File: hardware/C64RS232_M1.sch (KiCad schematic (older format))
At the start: 9 parts, among them J1 C64 USER PORT, J2 DE-9 FEMALE / DTE, U1 MAX3243

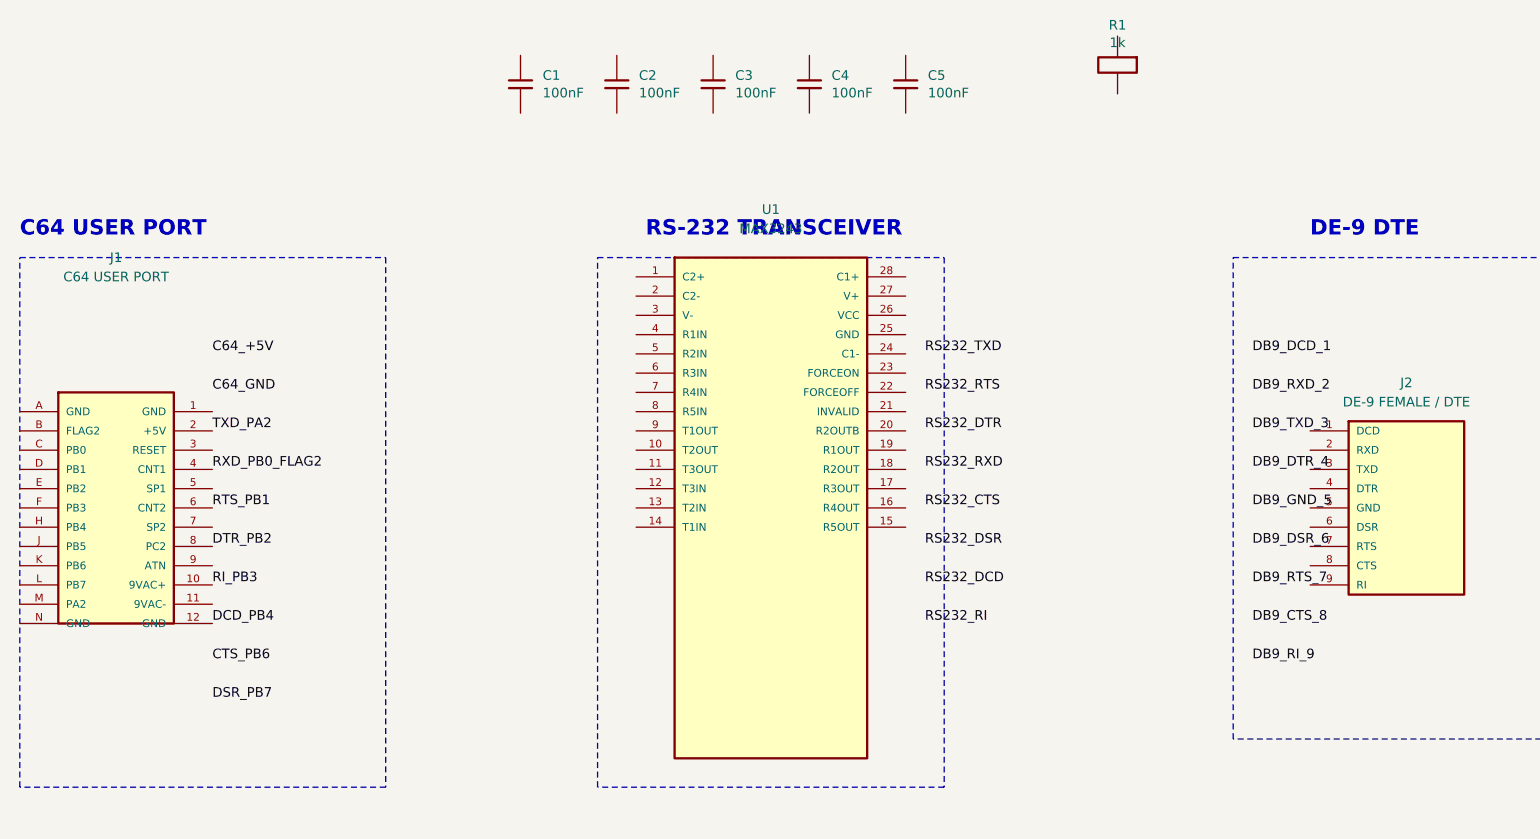
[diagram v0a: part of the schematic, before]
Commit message: Generate electrically connected KiCad M1.8 schematic
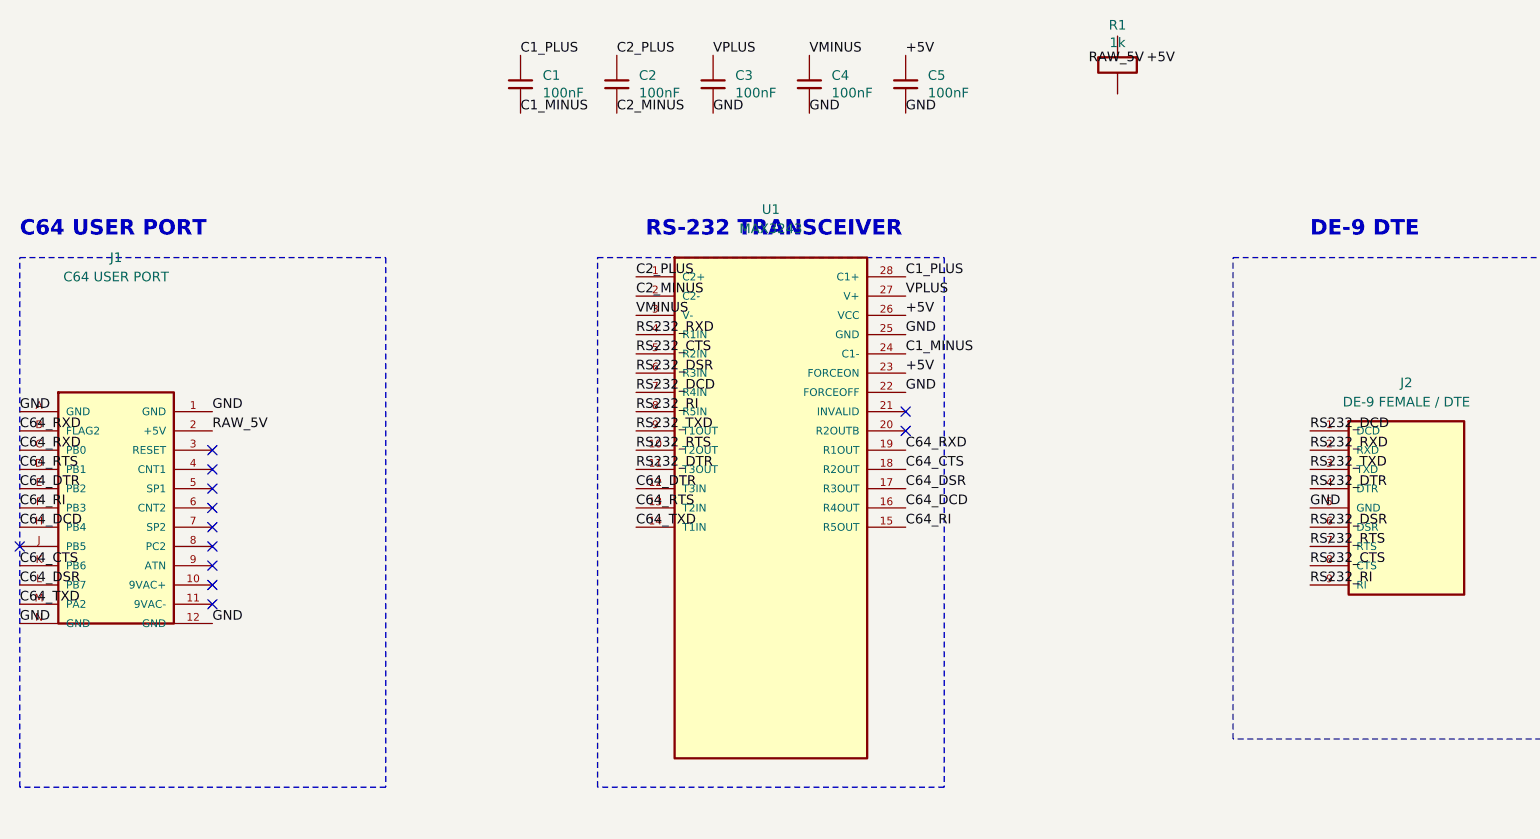
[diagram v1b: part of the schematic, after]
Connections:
- net DCD_PB4 is gone; now on net GND: J1.12 (GND)
- net RS232_CTS: now also J2.8 (CTS), U1.5 (R2IN)
- net RS232_DCD: now also J2.1 (DCD), U1.7 (R4IN)
- net RS232_DSR: now also J2.6 (DSR), U1.6 (R3IN)
- net RS232_DTR: now also J2.4 (DTR), U1.11 (T3OUT)
- net RS232_RI: now also J2.9 (RI), U1.8 (R5IN)
- net RS232_RTS: now also J2.7 (RTS), U1.10 (T2OUT)
- net RS232_RXD: now also J2.2 (RXD), U1.4 (R1IN)
- net RS232_TXD: now also J2.3 (TXD), U1.9 (T1OUT)
- net GND: now reaches J1.1 (GND)
- net GND: now also C3.2, C4.2, C5.2, J1.A (GND), J1.N (GND), J2.5 (GND), U1.22 (FORCEOFF), U1.25 (GND)
- net C64_RXD: now reaches J1.B (FLAG2)
- net C64_RXD: now also J1.C (PB0), U1.19 (R1OUT)
- net C64_RTS: now reaches J1.D (PB1)
- net C64_RTS: now also U1.13 (T2IN)
- net C64_DTR: now reaches J1.E (PB2)
- net C64_DTR: now also U1.12 (T3IN)
- net C64_RI: now reaches J1.F (PB3)
- net C64_RI: now also U1.15 (R5OUT)
- net C64_DCD: now reaches J1.H (PB4)
- net C64_DCD: now also U1.16 (R4OUT)
- net C64_CTS: now reaches J1.K (PB6)
- net C64_CTS: now also U1.18 (R2OUT)
- net C64_DSR: now reaches J1.L (PB7)
- net C64_DSR: now also U1.17 (R3OUT)
- net C64_TXD: now reaches J1.M (PA2)
- net C64_TXD: now also U1.14 (T1IN)
- net C2_PLUS: now reaches U1.1 (C2+)
- net C2_PLUS: now also C2.1
- net C2_MINUS: now reaches U1.2 (C2-)
- net C2_MINUS: now also C2.2
- net +5V: now reaches U1.23 (FORCEON)
- net +5V: now also C5.1, U1.26 (VCC)
- net C1_MINUS: now reaches U1.24 (C1-)
- net C1_MINUS: now also C1.2
- net VPLUS: now reaches U1.27 (V+)
- net VPLUS: now also C3.1
- net C1_PLUS: now reaches U1.28 (C1+)
- net C1_PLUS: now also C1.1
- net VMINUS: now reaches U1.3 (V-)
- net VMINUS: now also C4.1
- net DTR_PB2: no longer names the net of J1.8 (PC2)
- net RI_PB3: no longer names the net of J1.10 (9VAC+)
- net RTS_PB1: no longer names the net of J1.6 (CNT2)
- net RXD_PB0_FLAG2: no longer names the net of J1.4 (CNT1)
- net TXD_PA2 renamed RAW_5V
- no-connect marks 0 -> 12
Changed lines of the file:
@@
 Title "C64RS232 User Port to RS-232"
 Date "2026-09-14"
-Rev "M1"
+Rev "M1.8"
 Comp "Ploos-AS"
 Comment1 "C64 User Port / MAX3243 / DE-9 DTE"
 Comment2 "SLIP-capable architecture"
-Comment3 "M1 schematic baseline"
+Comment3 "M1.8 electrically connected baseline"
 Comment4 "Verify against datasheets before manufacture"
 $EndDescr
@@
 Text Notes 1400 6200 0 60 ~ 12
 This is an M1 design baseline; ERC/DRC and manufacturer-specific footprint checks remain required.
-Text Label 2300 3000 0 50 ~ 0
-C64_+5V
-Text Label 2300 3200 0 50 ~ 0
-C64_GND
+Text Label 1300 4300 0 50 ~ 0
+C64_TXD
+Text Label 4500 3900 0 50 ~ 0
+C64_TXD
+Text Label 1300 3600 0 50 ~ 0
+C64_RTS
+Text Label 4500 3800 0 50 ~ 0
+C64_RTS
+Text Label 1300 3700 0 50 ~ 0
+C64_DTR
+Text Label 4500 3700 0 50 ~ 0
+C64_DTR
+Text Label 1300 3500 0 50 ~ 0
+C64_RXD
+Text Label 1300 3400 0 50 ~ 0
+C64_RXD
+Text Label 5900 3500 0 50 ~ 0
+C64_RXD
+Text Label 1300 4100 0 50 ~ 0
+C64_CTS
+Text Label 5900 3600 0 50 ~ 0
+C64_CTS
+Text Label 1300 4200 0 50 ~ 0
+C64_DSR
+Text Label 5900 3700 0 50 ~ 0
+C64_DSR
+Text Label 1300 3900 0 50 ~ 0
+C64_DCD
+Text Label 5900 3800 0 50 ~ 0
+C64_DCD
+Text Label 1300 3800 0 50 ~ 0
+C64_RI
+Text Label 5900 3900 0 50 ~ 0
+C64_RI
+Text Label 4500 3400 0 50 ~ 0
+RS232_TXD
+Text Label 8000 3600 0 50 ~ 0
+RS232_TXD
+Text Label 4500 3500 0 50 ~ 0
+RS232_RTS
+Text Label 8000 4000 0 50 ~ 0
+RS232_RTS
+Text Label 4500 3600 0 50 ~ 0
+RS232_DTR
+Text Label 8000 3700 0 50 ~ 0
+RS232_DTR
+Text Label 4500 2900 0 50 ~ 0
+RS232_RXD
+Text Label 8000 3500 0 50 ~ 0
+RS232_RXD
+Text Label 4500 3000 0 50 ~ 0
+RS232_CTS
+Text Label 8000 4100 0 50 ~ 0
+RS232_CTS
+Text Label 4500 3100 0 50 ~ 0
+RS232_DSR
+Text Label 8000 3900 0 50 ~ 0
+RS232_DSR
+Text Label 4500 3200 0 50 ~ 0
+RS232_DCD
+Text Label 8000 3400 0 50 ~ 0
+RS232_DCD
+Text Label 4500 3300 0 50 ~ 0
+RS232_RI
+Text Label 8000 4200 0 50 ~ 0
+RS232_RI
 Text Label 2300 3400 0 50 ~ 0
-TXD_PA2
-Text Label 2300 3600 0 50 ~ 0
-RXD_PB0_FLAG2
-Text Label 2300 3800 0 50 ~ 0
-RTS_PB1
-Text Label 2300 4000 0 50 ~ 0
-DTR_PB2
-Text Label 2300 4200 0 50 ~ 0
-RI_PB3
+RAW_5V
+Text Label 6850 1500 0 50 ~ 0
+RAW_5V
+Text Label 7150 1500 0 50 ~ 0
++5V
+Text Label 5900 2800 0 50 ~ 0
++5V
+Text Label 5900 3100 0 50 ~ 0
++5V
+Text Label 5900 1450 0 50 ~ 0
++5V
+Text Label 2300 3300 0 50 ~ 0
+GND
 Text Label 2300 4400 0 50 ~ 0
-DCD_PB4
-Text Label 2300 4600 0 50 ~ 0
-CTS_PB6
-Text Label 2300 4800 0 50 ~ 0
-DSR_PB7
-Text Label 6000 3000 0 50 ~ 0
-RS232_TXD
-Text Label 6000 3200 0 50 ~ 0
-RS232_RTS
-Text Label 6000 3400 0 50 ~ 0
-RS232_DTR
-Text Label 6000 3600 0 50 ~ 0
-RS232_RXD
-Text Label 6000 3800 0 50 ~ 0
-RS232_CTS
-Text Label 6000 4000 0 50 ~ 0
-RS232_DSR
-Text Label 6000 4200 0 50 ~ 0
-RS232_DCD
-Text Label 6000 4400 0 50 ~ 0
-RS232_RI
-Text Label 7700 3000 0 50 ~ 0
-DB9_DCD_1
-Text Label 7700 3200 0 50 ~ 0
-DB9_RXD_2
-Text Label 7700 3400 0 50 ~ 0
-DB9_TXD_3
-Text Label 7700 3600 0 50 ~ 0
-DB9_DTR_4
-Text Label 7700 3800 0 50 ~ 0
-DB9_GND_5
-Text Label 7700 4000 0 50 ~ 0
-DB9_DSR_6
-Text Label 7700 4200 0 50 ~ 0
-DB9_RTS_7
-Text Label 7700 4400 0 50 ~ 0
-DB9_CTS_8
-Text Label 7700 4600 0 50 ~ 0
-DB9_RI_9
+GND
+Text Label 1300 3300 0 50 ~ 0
+GND
+Text Label 1300 4400 0 50 ~ 0
+GND
+Text Label 5900 2900 0 50 ~ 0
+GND
+Text Label 5900 3200 0 50 ~ 0
+GND
+Text Label 8000 3800 0 50 ~ 0
+GND
+Text Label 4900 1750 0 50 ~ 0
+GND
+Text Label 5400 1750 0 50 ~ 0
+GND
+Text Label 5900 1750 0 50 ~ 0
+GND
+Text Label 3900 1450 0 50 ~ 0
+C1_PLUS
+Text Label 5900 2600 0 50 ~ 0
+C1_PLUS
+Text Label 3900 1750 0 50 ~ 0
+C1_MINUS
+Text Label 5900 3000 0 50 ~ 0
+C1_MINUS
+Text Label 4400 1450 0 50 ~ 0
+C2_PLUS
+Text Label 4500 2600 0 50 ~ 0
+C2_PLUS
+Text Label 4400 1750 0 50 ~ 0
+C2_MINUS
+Text Label 4500 2700 0 50 ~ 0
+C2_MINUS
+Text Label 4900 1450 0 50 ~ 0
+VPLUS
+Text Label 5900 2700 0 50 ~ 0
+VPLUS
+Text Label 5400 1450 0 50 ~ 0
+VMINUS
+Text Label 4500 2800 0 50 ~ 0
+VMINUS
+NoConn ~ 2300 3500
+NoConn ~ 2300 3600
+NoConn ~ 2300 3700
+NoConn ~ 2300 3800
+NoConn ~ 2300 3900
+NoConn ~ 2300 4000
+NoConn ~ 2300 4100
+NoConn ~ 2300 4200
+NoConn ~ 2300 4300
+NoConn ~ 1300 4000
+NoConn ~ 5900 3400
+NoConn ~ 5900 3300
 Wire Notes Line
 	1300 2500 3200 2500

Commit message: Generate electrically connected KiCad M1.8 schematic
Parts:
- F1: renamed from R1; value 1k -> 100mA PTC
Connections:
- net +5V: now also F1.2
- net RAW_5V: now also F1.1
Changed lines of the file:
@@
 $EndComp
 $Comp
-L R R1
+L R F1
 U 1 1 9
 P 7000 1500
-F 0 "R1" V 6793 1500 50 0000 C CNN
-F 1 "1k" V 6884 1500 50 0000 C CNN
+F 0 "F1" V 6793 1500 50 0000 C CNN
+F 1 "100mA PTC" V 6884 1500 50 0000 C CNN
 	1    7000 1500
 	0 1 1 0
@@
 Text Label 2300 3400 0 50 ~ 0
 RAW_5V
-Text Label 6850 1500 0 50 ~ 0
+Text Label 7000 1350 0 50 ~ 0
 RAW_5V
-Text Label 7150 1500 0 50 ~ 0
+Text Label 7000 1650 0 50 ~ 0
 +5V
 Text Label 5900 2800 0 50 ~ 0

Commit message: Generate electrically connected KiCad M1.8 schematic
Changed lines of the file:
@@
 Wire Notes Line
 	7600 5000 7600 2500
+$Comp
+L PWR_FLAG #FLG0101
+U 1 1 10
+P 7500 1650
+F 0 "#FLG0101" H 7500 1725 50 0001 C CNN
+F 1 "PWR_FLAG" H 7500 1823 50 0000 C CNN
+	1    7500 1650
+	1    0    0    -1
+$EndComp
+Text Label 7500 1650 0 50 ~ 0
++5V
 $EndSCHEMATC

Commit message: Generate electrically connected KiCad M1.8 schematic
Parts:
- C1: value 100nF -> 47nF
- C2, C3, C4: value 100nF -> 330nF
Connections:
- net +5V: now also U1.22 (FORCEOFF)
- net GND: no longer U1.22 (FORCEOFF)
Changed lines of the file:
@@
 Title "C64RS232 User Port to RS-232"
 Date "2026-09-14"
-Rev "M1.8"
+Rev "M1.9"
 Comp "Ploos-AS"
 Comment1 "C64 User Port / MAX3243 / DE-9 DTE"
 Comment2 "SLIP-capable architecture"
-Comment3 "M1.8 electrically connected baseline"
+Comment3 "M1.9 MAX3243E 5V baseline"
 Comment4 "Verify against datasheets before manufacture"
 $EndDescr
@@
 P 3900 1600
 F 0 "C1" H 4015 1646 50 0000 L CNN
-F 1 "100nF" H 4015 1555 50 0000 L CNN
+F 1 "47nF" H 4015 1555 50 0000 L CNN
 	1    3900 1600
 	1 0 0 -1
@@
 P 4400 1600
 F 0 "C2" H 4515 1646 50 0000 L CNN
-F 1 "100nF" H 4515 1555 50 0000 L CNN
+F 1 "330nF" H 4515 1555 50 0000 L CNN
 	1    4400 1600
 	1 0 0 -1
@@
 P 4900 1600
 F 0 "C3" H 5015 1646 50 0000 L CNN
-F 1 "100nF" H 5015 1555 50 0000 L CNN
+F 1 "330nF" H 5015 1555 50 0000 L CNN
 	1    4900 1600
 	1 0 0 -1
@@
 P 5400 1600
 F 0 "C4" H 5515 1646 50 0000 L CNN
-F 1 "100nF" H 5515 1555 50 0000 L CNN
+F 1 "330nF" H 5515 1555 50 0000 L CNN
 	1    5400 1600
 	1 0 0 -1
@@
 Text Label 5900 3100 0 50 ~ 0
 +5V
+Text Label 5900 3200 0 50 ~ 0
++5V
 Text Label 5900 1450 0 50 ~ 0
 +5V
@@
 Text Label 5900 2900 0 50 ~ 0
 GND
-Text Label 5900 3200 0 50 ~ 0
-GND
 Text Label 8000 3800 0 50 ~ 0

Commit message: Generate M1.10 KiCad schematic baseline
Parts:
- C1, C2, C3, C4, C5: footprint (none) -> Capacitor_SMD:C_0805_2012Metric_Pad1.18x1.45mm_HandSolder
- F1: value 100mA PTC -> 1206L010/30WR; footprint (none) -> Fuse:Fuse_1206_3216Metric_Pad1.42x1.75mm_HandSolder
- J1: footprint (none) -> C64RS232:C64_User_Port_Edge
- J2: value DE-9 FEMALE / DTE -> 5747844-4; footprint (none) -> Connector_Dsub:DSUB-9_Female_Horizontal_P2.77x2.84mm_EdgePinOffset9.40mm_Housed_MountingHolesOffset11.32mm
- U1: value MAX3243 -> MAX3243EIPWR; footprint (none) -> Package_SO:TSSOP-28_4.4x9.7mm_P0.65mm
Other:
- note added: "FORCEON and FORCEOFF are tied high for normal always-on operation."
- note removed: "FORCEON is tied high and FORCEOFF low for normal always-on operation."
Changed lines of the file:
@@
 Title "C64RS232 User Port to RS-232"
 Date "2026-09-14"
-Rev "M1.9"
+Rev "M1.10"
 Comp "Ploos-AS"
 Comment1 "C64 User Port / MAX3243 / DE-9 DTE"
 Comment2 "SLIP-capable architecture"
-Comment3 "M1.9 MAX3243E 5V baseline"
+Comment3 "M1.10 frozen footprint baseline"
 Comment4 "Verify against datasheets before manufacture"
 $EndDescr
@@
 F 0 "J1" H 1800 5100 50  0000 C CNN
 F 1 "C64 USER PORT" H 1800 5000 50 0000 C CNN
+F 2 "C64RS232:C64_User_Port_Edge" H 0 0 50 0001 C CNN
 	1    1800 3800
 	1 0 0 -1
@@
 P 5200 3800
 F 0 "U1" H 5200 5350 50 0000 C CNN
-F 1 "MAX3243" H 5200 5250 50 0000 C CNN
+F 1 "MAX3243EIPWR" H 0 0 50 0000 C CNN
+F 2 "Package_SO:TSSOP-28_4.4x9.7mm_P0.65mm" H 0 0 50 0001 C CNN
 	1    5200 3800
 	1 0 0 -1
@@
 P 8500 3800
 F 0 "J2" H 8500 4450 50 0000 C CNN
-F 1 "DE-9 FEMALE / DTE" H 8500 4350 50 0000 C CNN
+F 1 "5747844-4" H 0 0 50 0000 C CNN
+F 2 "Connector_Dsub:DSUB-9_Female_Horizontal_P2.77x2.84mm_EdgePinOffset9.40mm_Housed_MountingHolesOffset11.32mm" H 0 0 50 0001 C CNN
 	1    8500 3800
 	1 0 0 -1
@@
 F 0 "C1" H 4015 1646 50 0000 L CNN
 F 1 "47nF" H 4015 1555 50 0000 L CNN
+F 2 "Capacitor_SMD:C_0805_2012Metric_Pad1.18x1.45mm_HandSolder" H 0 0 50 0001 C CNN
 	1    3900 1600
 	1 0 0 -1
@@
 F 0 "C2" H 4515 1646 50 0000 L CNN
 F 1 "330nF" H 4515 1555 50 0000 L CNN
+F 2 "Capacitor_SMD:C_0805_2012Metric_Pad1.18x1.45mm_HandSolder" H 0 0 50 0001 C CNN
 	1    4400 1600
 	1 0 0 -1
@@
 F 0 "C3" H 5015 1646 50 0000 L CNN
 F 1 "330nF" H 5015 1555 50 0000 L CNN
+F 2 "Capacitor_SMD:C_0805_2012Metric_Pad1.18x1.45mm_HandSolder" H 0 0 50 0001 C CNN
 	1    4900 1600
 	1 0 0 -1
@@
 F 0 "C4" H 5515 1646 50 0000 L CNN
 F 1 "330nF" H 5515 1555 50 0000 L CNN
+F 2 "Capacitor_SMD:C_0805_2012Metric_Pad1.18x1.45mm_HandSolder" H 0 0 50 0001 C CNN
 	1    5400 1600
 	1 0 0 -1
@@
 F 0 "C5" H 6015 1646 50 0000 L CNN
 F 1 "100nF" H 6015 1555 50 0000 L CNN
+F 2 "Capacitor_SMD:C_0805_2012Metric_Pad1.18x1.45mm_HandSolder" H 0 0 50 0001 C CNN
 	1    5900 1600
 	1 0 0 -1
@@
 P 7000 1500
 F 0 "F1" V 6793 1500 50 0000 C CNN
-F 1 "100mA PTC" V 6884 1500 50 0000 C CNN
+F 1 "1206L010/30WR" H 0 0 50 0000 C CNN
+F 2 "Fuse:Fuse_1206_3216Metric_Pad1.42x1.75mm_HandSolder" H 0 0 50 0001 C CNN
 	1    7000 1500
 	0 1 1 0
@@
 MAX3243 provides 3 drivers / 5 receivers, matching TXD/RTS/DTR and RXD/CTS/DSR/DCD/RI.
 Text Notes 1400 6050 0 60 ~ 12
-FORCEON is tied high and FORCEOFF low for normal always-on operation.
+FORCEON and FORCEOFF are tied high for normal always-on operation.
 Text Notes 1400 6200 0 60 ~ 12
 This is an M1 design baseline; ERC/DRC and manufacturer-specific footprint checks remain required.

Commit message: Generate M1.10 KiCad schematic baseline
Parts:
- J2: footprint Connector_Dsub:DSUB-9_Female_Horizontal_P2.77x2.84mm_EdgePinOffset9.40mm_Housed_MountingHolesOffset11.32mm -> C64RS232:TE_5747844-4
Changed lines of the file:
@@
 F 0 "J2" H 8500 4450 50 0000 C CNN
 F 1 "5747844-4" H 0 0 50 0000 C CNN
-F 2 "Connector_Dsub:DSUB-9_Female_Horizontal_P2.77x2.84mm_EdgePinOffset9.40mm_Housed_MountingHolesOffset11.32mm" H 0 0 50 0001 C CNN
+F 2 "C64RS232:TE_5747844-4" H 0 0 50 0001 C CNN
 	1    8500 3800
 	1 0 0 -1
